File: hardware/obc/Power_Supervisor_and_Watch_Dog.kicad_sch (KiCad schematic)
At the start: 23 parts, among them Q51 IRF7306, Q52 PMBT2222A, Q53 MBT2222ADW1T1, Q54 MBT2222ADW1T1

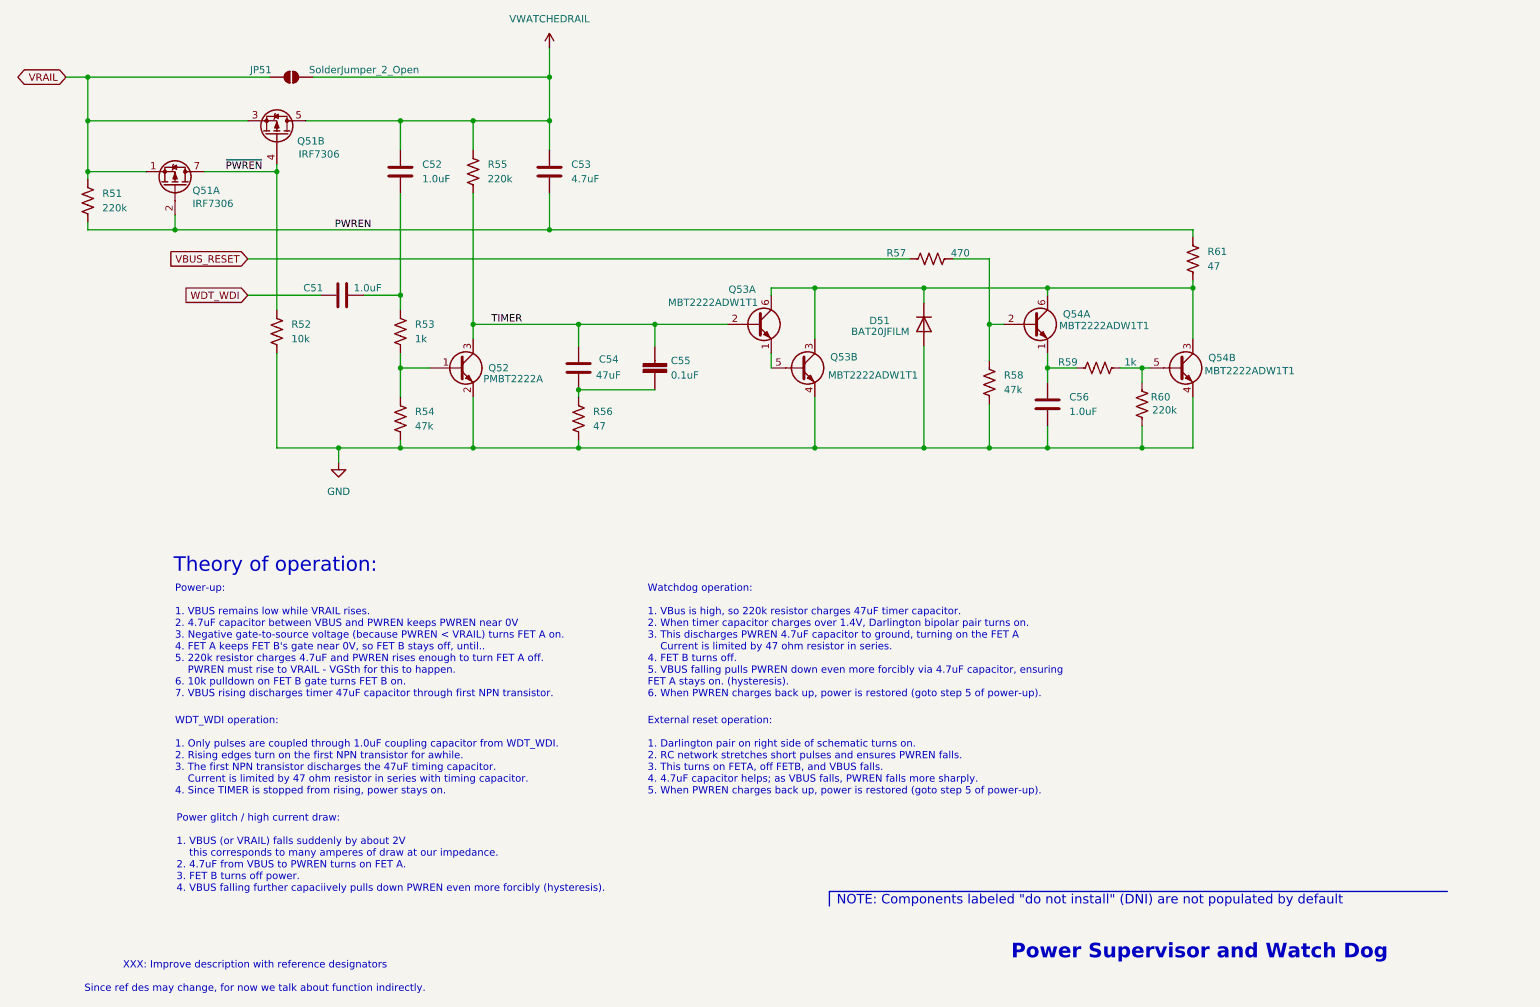
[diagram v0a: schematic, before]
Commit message: obc: Many schematic cleanups
Mostly alignment of components, adjustment of text.

Change SPI resistors to 27 ohms.
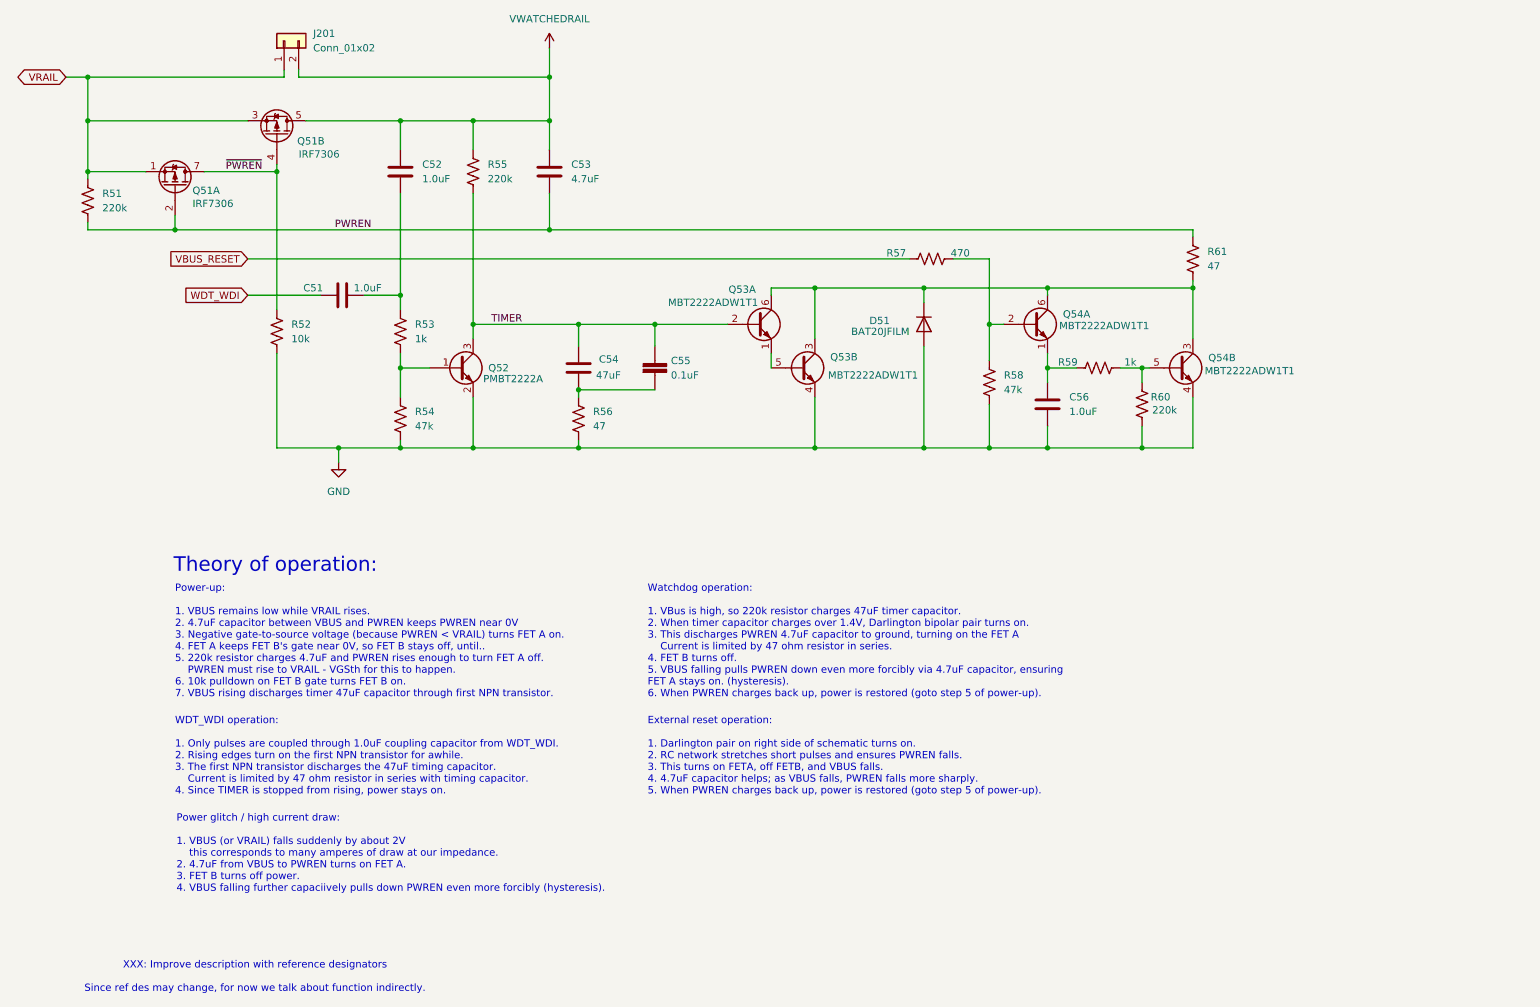
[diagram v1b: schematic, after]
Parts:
- removed JP51: SolderJumper_2_Open, Jumper:SolderJumper-2_P1.3mm_Open_TrianglePad1.0x1.5mm, symbol Jumper:SolderJumper_2_Open
- added J201: Conn_01x02, Connector_PinHeader_2.00mm:PinHeader_1x02_P2.00mm_Vertical, symbol Connector_Generic:Conn_01x02
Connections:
- net VRAIL: now also J201.1 (Pin_1)
- net VWATCHEDRAIL: now also J201.2 (Pin_2)
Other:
- note removed: "NOTE: Components labeled "do not install" (DNI) are not populated by default"
- note removed: "Power Supervisor and Watch Dog"
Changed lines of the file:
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@@
 		(rev "1")
 		(company "Luke Titi, Michael Lyle")
+		(comment 2 "NOTE: Components labeled \"do not install\" (DNI) are not populated by default")
 	)
 	(junction
@@
 	(wire
 		(pts
-			(xy 68.58 26.67) (xy 109.855 26.67)
-		)
-		(stroke
-			(width 0)
-			(type default)
-		)
-	)
-	(wire
-		(pts
 			(xy 96.52 34.29) (xy 109.855 34.29)
 		)
@@
 	(wire
 		(pts
-			(xy 29.21 26.67) (xy 60.96 26.67)
+			(xy 29.21 26.67) (xy 63.5 26.67)
 		)
 		(stroke
@@
 		)
 	)
-	(polyline
-		(pts
-			(xy 158.75 171.45) (xy 158.75 168.91)
-		)
-		(stroke
-			(width 0)
-			(type default)
-		)
-	)
 	(wire
 		(pts
@@
 	(wire
 		(pts
+			(xy 66.04 25.4) (xy 66.04 26.67)
+		)
+		(stroke
+			(width 0)
+			(type default)
+		)
+	)
+	(wire
+		(pts
 			(xy 62.23 74.93) (xy 62.23 91.44)
 		)
@@
 	(wire
 		(pts
+			(xy 63.5 25.4) (xy 63.5 26.67)
+		)
+		(stroke
+			(width 0)
+			(type default)
+		)
+	)
+	(wire
+		(pts
 			(xy 29.21 43.18) (xy 29.21 34.29)
 		)
@@
 	(wire
 		(pts
+			(xy 66.04 26.67) (xy 109.855 26.67)
+		)
+		(stroke
+			(width 0)
+			(type default)
+		)
+	)
+	(wire
+		(pts
 			(xy 67.31 34.29) (xy 83.82 34.29)
 		)
@@
 		(pts
 			(xy 148.59 74.93) (xy 148.59 77.47)
-		)
-		(stroke
-			(width 0)
-			(type default)
-		)
-	)
-	(polyline
-		(pts
-			(xy 158.75 168.91) (xy 266.7 168.91)
 		)
 		(stroke
@@
 			)
 			(justify left top)
-		)
-	)
-	(text "Power Supervisor and Watch Dog\n"
-		(exclude_from_sim no)
-		(at 190.5 180.975 0)
-		(effects
-			(font
-				(size 2.54 2.54)
-				(thickness 1.016)
-				(bold yes)
-			)
-			(justify left bottom)
-		)
-	)
-	(text "NOTE: Components labeled \"do not install\" (DNI) are not populated by default"
-		(exclude_from_sim no)
-		(at 160.02 171.45 0)
-		(effects
-			(font
-				(size 1.651 1.651)
-			)
-			(justify left bottom)
 		)
 	)
@@
 	)
 	(symbol
-		(lib_id "Jumper:SolderJumper_2_Open")
-		(at 64.77 26.67 0)
-		(unit 1)
-		(exclude_from_sim yes)
-		(in_bom no)
-		(on_board yes)
-		(dnp no)
-		(property "Reference" "JP51"
-			(at 59.436 25.4 0)
-			(effects
-				(font
-					(size 1.27 1.27)
-				)
-			)
-		)
-		(property "Value" "SolderJumper_2_Open"
-			(at 77.47 25.4 0)
-			(effects
-				(font
-					(size 1.27 1.27)
-				)
-			)
-		)
-		(property "Footprint" "Jumper:SolderJumper-2_P1.3mm_Open_TrianglePad1.0x1.5mm"
-			(at 64.77 26.67 0)
-			(effects
-				(font
-					(size 1.27 1.27)
-				)
-				(hide yes)
-			)
-		)
-		(property "Datasheet" "~"
-			(at 64.77 26.67 0)
-			(effects
-				(font
-					(size 1.27 1.27)
-				)
-				(hide yes)
-			)
-		)
-		(property "Description" "Solder Jumper, 2-pole, open"
-			(at 64.77 26.67 0)
-			(effects
-				(font
-					(size 1.27 1.27)
-				)
-				(hide yes)
-			)
-		)
-		(pin "2"
-		)
-		(pin "1"
-		)
-		(instances
-			(project ""
-				(path "/e3ac22ea-6806-4807-a025-571315789c25/0ba89562-211f-497f-9372-6f77bd1df388"
-					(reference "JP51")
-					(unit 1)
-				)
-			)
-		)
-	)
-	(symbol
 		(lib_id "Device:R_US")
 		(at 62.23 71.12 0)
@@
 					(unit 1)
 				)
+			)
+		)
+	)
+	(symbol
+		(lib_id "Connector_Generic:Conn_01x02")
+		(at 63.5 20.32 90)
+		(unit 1)
+		(exclude_from_sim no)
+		(in_bom yes)
+		(on_board yes)
+		(dnp no)
+		(fields_autoplaced yes)
+		(property "Reference" "J201"
+			(at 68.58 19.0499 90)
+			(effects
+				(font
+					(size 1.27 1.27)
+				)
+				(justify right)
+			)
+		)
+		(property "Value" "Conn_01x02"
+			(at 68.58 21.5899 90)
+			(effects
+				(font
+					(size 1.27 1.27)
+				)
+				(justify right)
+			)
+		)
+		(property "Footprint" "Connector_PinHeader_2.00mm:PinHeader_1x02_P2.00mm_Vertical"
+			(at 63.5 20.32 0)
+			(effects
+				(font
+					(size 1.27 1.27)
+				)
+				(hide yes)
+			)
+		)
+		(property "Datasheet" "~"
+			(at 63.5 20.32 0)
+			(effects
+				(font
+					(size 1.27 1.27)
+				)
+				(hide yes)
+			)
+		)
+		(property "Description" "Generic connector, single row, 01x02, script generated (kicad-library-utils/schlib/autogen/connector/)"
+			(at 63.5 20.32 0)
+			(effects
+				(font
+					(size 1.27 1.27)
+				)
+				(hide yes)
+			)
+		)
+		(pin "1"
+		)
+		(pin "2"
+		)
+		(instances
+			(project ""
+				(path "/e3ac22ea-6806-4807-a025-571315789c25/0ba89562-211f-497f-9372-6f77bd1df388"
+					(reference "J201")
+					(unit 1)
+				)

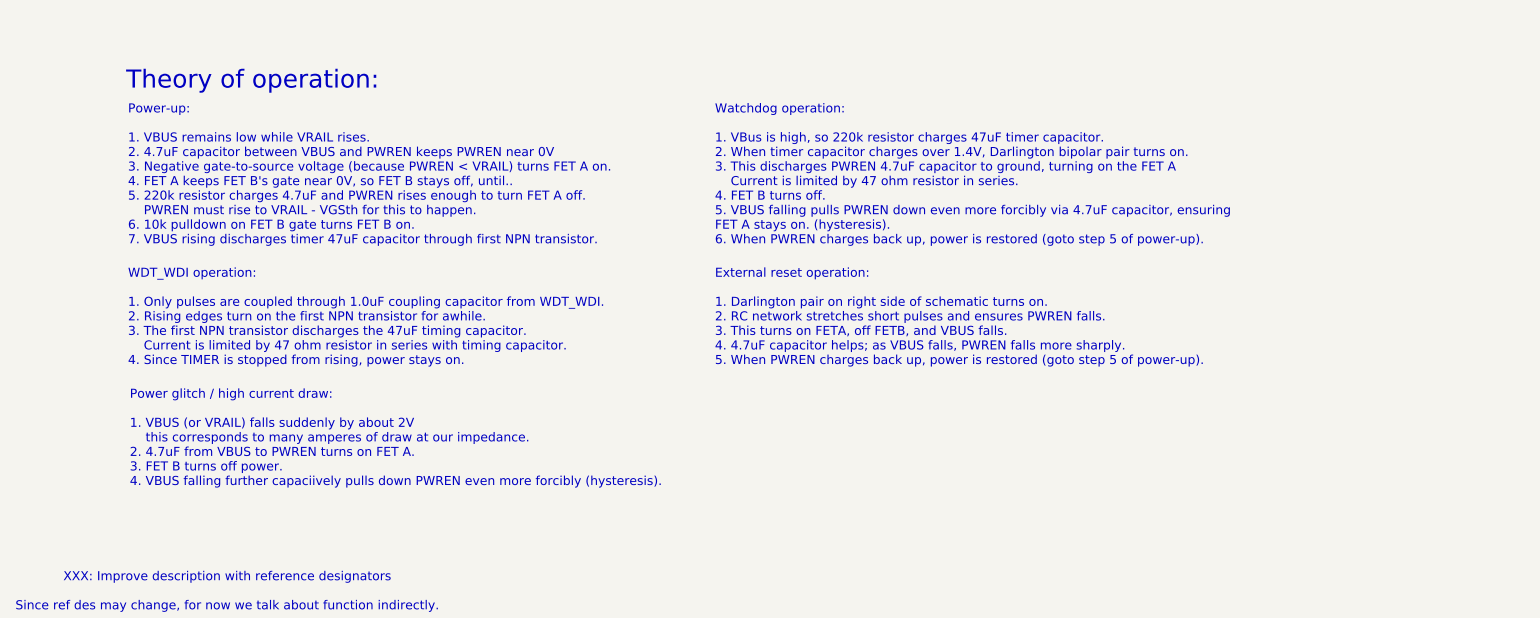
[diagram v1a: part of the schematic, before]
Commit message: obc: final (hopefully) design review for rev B
- Update some text
- Change some part values based on math (greater charge current)
- Increase design conservatism (place pullups on CS)

BOM review still needs to occur, including for a few parts that had
values changed in this pass (without part numbers being chosen)
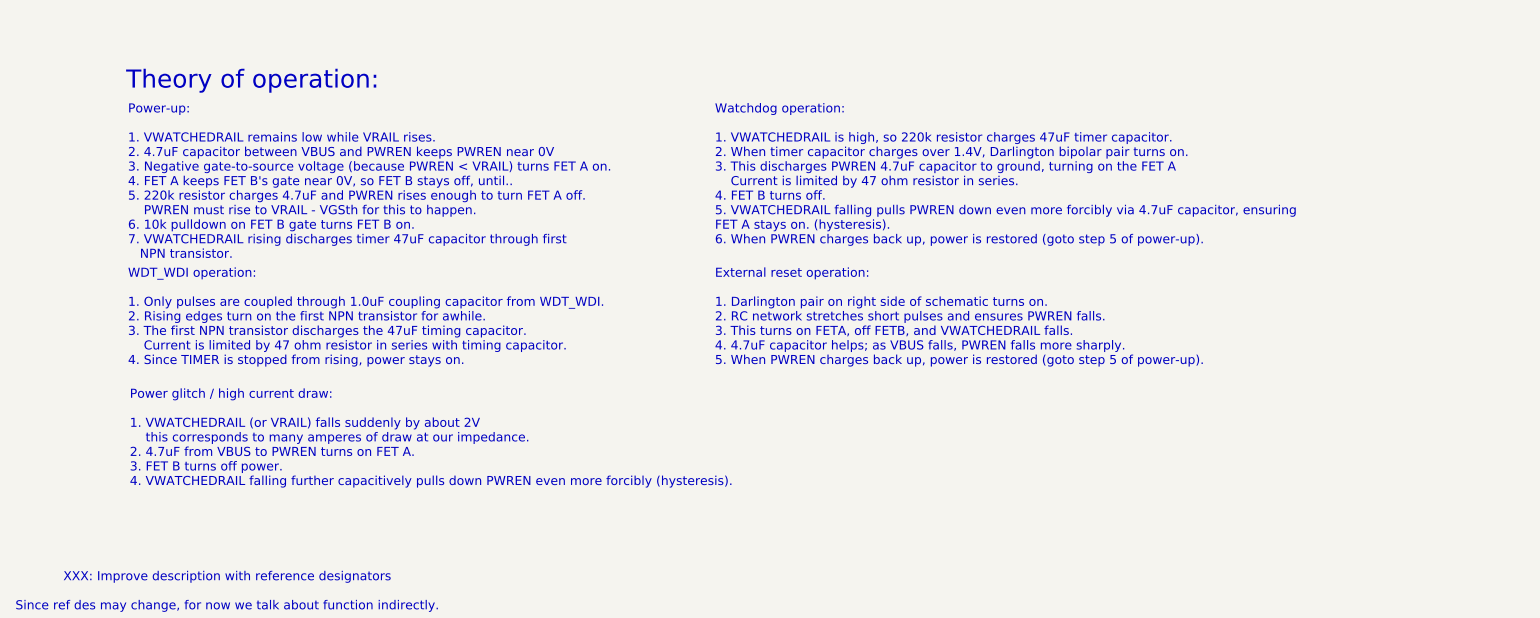
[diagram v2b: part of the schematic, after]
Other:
- note added: "External reset operation: 1. Darlington pair on right side of schematic turns on. 2. RC network stretches short pulses and ensures PWREN falls. 3. This turns on FETA, off FETB, and VWATCHEDRAIL falls. 4. 4.7uF capacitor helps; as VBUS falls, PWREN falls more sharply. 5. When PWREN charges back up, power is restored (goto step 5 of power-up)."
- note added: "Power glitch / high current draw: 1. VWATCHEDRAIL (or VRAIL) falls suddenly by about 2V this corresponds to many amperes of draw at our impedance. 2. 4.7uF from VBUS to PWREN turns on FET A. 3. FET B turns off power. 4. VWATCHEDRAIL falling further capacitively pulls down PWREN even more forcibly (hysteresis)."
- note added: "Power-up: 1. VWATCHEDRAIL remains low while VRAIL rises. 2. 4.7uF capacitor between VBUS and PWREN keeps PWREN near 0V 3. Negative gate-to-source voltage (because PWREN < VRAIL) turns FET A on. 4. FET A keeps FET B's gate near 0V, so FET B stays off, until.. 5. 220k resistor charges 4.7uF and PWREN rises enough to turn FET A off. PWREN must rise to VRAIL - VGSth for this to happen. 6. 10k pulldow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"
- note added: "Watchdog operation: 1. VWATCHEDRAIL is high, so 220k resistor charges 47uF timer capacitor. 2. When timer capacitor charges over 1.4V, Darlington bipolar pair turns on. 3. This discharges PWREN 4.7uF capacitor to ground, turning on the FET A Current is limited by 47 ohm resistor in series. 4. FET B turns off. 5. VWATCHEDRAIL falling pulls PWREN down even more forcibly via 4.7uF capacitor, ensurin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"
- note removed: "External reset operation: 1. Darlington pair on right side of schematic turns on. 2. RC network stretches short pulses and ensures PWREN falls. 3. This turns on FETA, off FETB, and VBUS falls. 4. 4.7uF capacitor helps; as VBUS falls, PWREN falls more sharply. 5. When PWREN charges back up, power is restored (goto step 5 of power-up)."
- note removed: "Power glitch / high current draw: 1. VBUS (or VRAIL) falls suddenly by about 2V this corresponds to many amperes of draw at our impedance. 2. 4.7uF from VBUS to PWREN turns on FET A. 3. FET B turns off power. 4. VBUS falling further capaciively pulls down PWREN even more forcibly (hysteresis)."
- note removed: "Power-up: 1. VBUS remains low while VRAIL rises. 2. 4.7uF capacitor between VBUS and PWREN keeps PWREN near 0V 3. Negative gate-to-source voltage (because PWREN < VRAIL) turns FET A on. 4. FET A keeps FET B's gate near 0V, so FET B stays off, until.. 5. 220k resistor charges 4.7uF and PWREN rises enough to turn FET A off. PWREN must rise to VRAIL - VGSth for this to happen. 6. 10k pulldown on FET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"
- note removed: "Watchdog operation: 1. VBus is high, so 220k resistor charges 47uF timer capacitor. 2. When timer capacitor charges over 1.4V, Darlington bipolar pair turns on. 3. This discharges PWREN 4.7uF capacitor to ground, turning on the FET A Current is limited by 47 ohm resistor in series. 4. FET B turns off. 5. VBUS falling pulls PWREN down even more forcibly via 4.7uF capacitor, ensuring FET A stays on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"
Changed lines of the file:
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@@
 		)
 	)
-	(text "External reset operation:\n\n1. Darlington pair on right side of schematic turns on.\n2. RC network stretches short pulses and ensures PWREN falls.\n3. This turns on FETA, off FETB, and VBUS falls.\n4. 4.7uF capacitor helps; as VBUS falls, PWREN falls more sharply.\n5. When PWREN charges back up, power is restored (goto step 5 of power-up)."
+	(text "External reset operation:\n\n1. Darlington pair on right side of schematic turns on.\n2. RC network stretches short pulses and ensures PWREN falls.\n3. This turns on FETA, off FETB, and VWATCHEDRAIL falls.\n4. 4.7uF capacitor helps; as VBUS falls, PWREN falls more sharply.\n5. When PWREN charges back up, power is restored (goto step 5 of power-up)."
 		(exclude_from_sim no)
 		(at 127 138.43 0)
@@
 		)
 	)
-	(text "Power glitch / high current draw:\n\n1. VBUS (or VRAIL) falls suddenly by about 2V\n	this corresponds to many amperes of draw at our impedance.\n2. 4.7uF from VBUS to PWREN turns on FET A.\n3. FET B turns off power.\n4. VBUS falling further capaciively pulls down PWREN even more forcibly (hysteresis)."
+	(text "Power glitch / high current draw:\n\n1. VWATCHEDRAIL (or VRAIL) falls suddenly by about 2V\n	this corresponds to many amperes of draw at our impedance.\n2. 4.7uF from VBUS to PWREN turns on FET A.\n3. FET B turns off power.\n4. VWATCHEDRAIL falling further capacitively pulls down PWREN even more forcibly (hysteresis)."
 		(exclude_from_sim no)
 		(at 44.704 155.448 0)
@@
 		)
 	)
-	(text "Watchdog operation:\n\n1. VBus is high, so 220k resistor charges 47uF timer capacitor.\n2. When timer capacitor charges over 1.4V, Darlington bipolar pair turns on.\n3. This discharges PWREN 4.7uF capacitor to ground, turning on the FET A\n	Current is limited by 47 ohm resistor in series.\n4. FET B turns off.\n5. VBUS falling pulls PWREN down even more forcibly via 4.7uF capacitor, ensuring\nFET A stays on. (hysteresis).\n6. When PWREN charges back up, power is restored (goto step 5 of power-up)."
+	(text "Watchdog operation:\n\n1. VWATCHEDRAIL is high, so 220k resistor charges 47uF timer capacitor.\n2. When timer capacitor charges over 1.4V, Darlington bipolar pair turns on.\n3. This discharges PWREN 4.7uF capacitor to ground, turning on the FET A\n	Current is limited by 47 ohm resistor in series.\n4. FET B turns off.\n5. VWATCHEDRAIL falling pulls PWREN down even more forcibly via 4.7uF capacitor, ensuring\nFET A stays on. (hysteresis).\n6. When PWREN charges back up, power is restored (goto step 5 of power-up)."
 		(exclude_from_sim no)
 		(at 127 115.316 0)
@@
 		)
 	)
-	(text "Power-up:\n\n1. VBUS remains low while VRAIL rises.\n2. 4.7uF capacitor between VBUS and PWREN keeps PWREN near 0V\n3. Negative gate-to-source voltage (because PWREN < VRAIL) turns FET A on.\n4. FET A keeps FET B's gate near 0V, so FET B stays off, until..\n5. 220k resistor charges 4.7uF and PWREN rises enough to turn FET A off.\n	PWREN must rise to VRAIL - VGSth for this to happen.\n6. 10k pulldown on FET B gate turns FET B on.\n7. VBUS rising discharges timer 47uF capacitor through first NPN transistor."
+	(text "Power-up:\n\n1. VWATCHEDRAIL remains low while VRAIL rises.\n2. 4.7uF capacitor between VBUS and PWREN keeps PWREN near 0V\n3. Negative gate-to-source voltage (because PWREN < VRAIL) turns FET A on.\n4. FET A keeps FET B's gate near 0V, so FET B stays off, until..\n5. 220k resistor charges 4.7uF and PWREN rises enough to turn FET A off.\n	PWREN must rise to VRAIL - VGSth for this to happen.\n6. 10k pulldown on FET B gate turns FET B on.\n7. VWATCHEDRAIL rising discharges timer 47uF capacitor through first\n   NPN transistor."
 		(exclude_from_sim no)
 		(at 44.45 115.316 0)
